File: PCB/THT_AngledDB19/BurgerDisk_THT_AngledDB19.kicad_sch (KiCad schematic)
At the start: 15 parts, among them J1 Daisy port in, J2 MicroSD module, J3 UART, J4 Daisy port out, U1 PC817

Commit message: Wider tracks for power
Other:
- company: (none) -> Colin Leroy-Mira
- title: (none) -> BurgerDisk PCB - Angled DB19 version
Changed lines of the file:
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@@
 (kicad_sch (version 20230121) (generator eeschema)
   (paper "A4")
+  (title_block
+    (title "BurgerDisk PCB - Angled DB19 version")
+    (date "2026-01-28")
+    (rev "v2")
+    (company "Colin Leroy-Mira")
+    (comment 1 "License: CC BY-SA")
+  )
   (junction (at 93.98 90.17) (diameter 0) (color 0 0 0 0)
   )

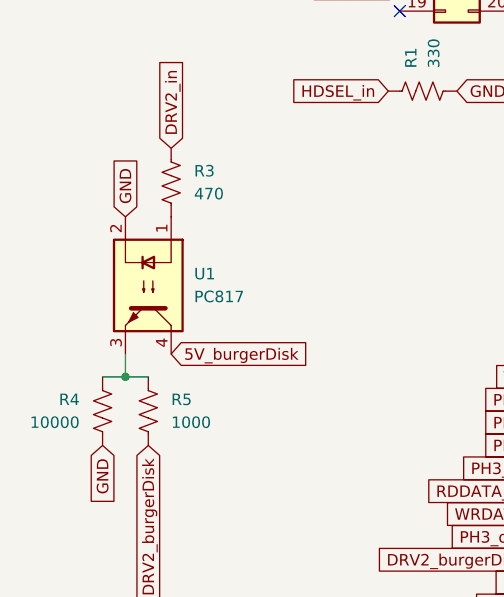
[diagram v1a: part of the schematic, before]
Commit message: Reverse 3 resistors for correct silkscreen orientation
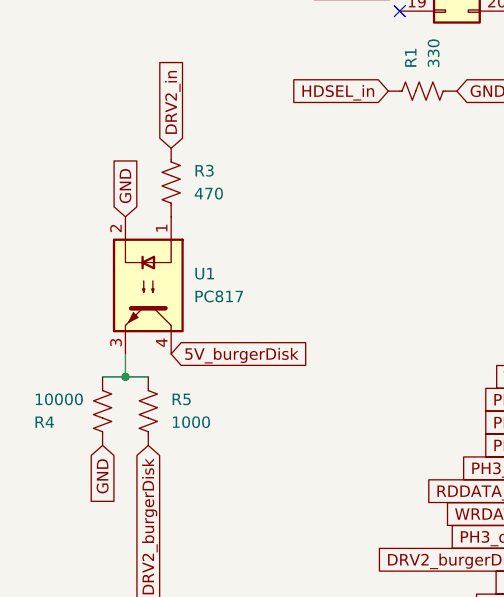
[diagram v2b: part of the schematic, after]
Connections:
- net DRV2_burgerDisk: now also R5.1; no longer R5.2
- net DRV2_in: now also R3.1; no longer R3.2
- net GND: now also R4.1; no longer R4.2
- net at U1.1: now also R3.2; no longer R3.1
- new net: R4.2, R5.2, U1.3
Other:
- moved on the sheet: R3, R4, R5
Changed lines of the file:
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@@
     )
   )
-  (symbol (lib_id "Device:R_US") (at 91.44 93.98 0) (unit 1)
+  (symbol (lib_id "Device:R_US") (at 91.44 93.98 180) (unit 1)
     (in_bom yes) (on_board yes) (dnp no)
-    (property "Reference" "R4" (at 88.9 92.71 0)
-      (effects (font (size 1.27 1.27)) (justify right))
-    )
-    (property "Value" "10000" (at 88.9 95.25 0)
-      (effects (font (size 1.27 1.27)) (justify right))
-    )
-    (property "Footprint" "Resistor_THT:R_Axial_DIN0207_L6.3mm_D2.5mm_P7.62mm_Horizontal" (at 92.456 94.234 90)
+    (property "Reference" "R4" (at 83.82 95.25 0)
+      (effects (font (size 1.27 1.27)) (justify right))
+    )
+    (property "Value" "10000" (at 83.82 92.71 0)
+      (effects (font (size 1.27 1.27)) (justify right))
+    )
+    (property "Footprint" "Resistor_THT:R_Axial_DIN0207_L6.3mm_D2.5mm_P7.62mm_Horizontal" (at 90.424 93.726 90)
       (effects (font (size 1.27 1.27)) hide)
     )
@@
     )
   )
-  (symbol (lib_id "Device:R_US") (at 99.06 68.58 180) (unit 1)
+  (symbol (lib_id "Device:R_US") (at 99.06 68.58 0) (unit 1)
     (in_bom yes) (on_board yes) (dnp no) (fields_autoplaced)
     (property "Reference" "R3" (at 101.6 67.31 0)
-      (effects (font (size 1.27 1.27)) (justify right))
+      (effects (font (size 1.27 1.27)) (justify left))
     )
     (property "Value" "470" (at 101.6 69.85 0)
-      (effects (font (size 1.27 1.27)) (justify right))
-    )
-    (property "Footprint" "Resistor_THT:R_Axial_DIN0309_L9.0mm_D3.2mm_P12.70mm_Horizontal" (at 98.044 68.326 90)
+      (effects (font (size 1.27 1.27)) (justify left))
+    )
+    (property "Footprint" "Resistor_THT:R_Axial_DIN0309_L9.0mm_D3.2mm_P12.70mm_Horizontal" (at 100.076 68.834 90)
       (effects (font (size 1.27 1.27)) hide)
     )
@@
     )
   )
-  (symbol (lib_id "Device:R_US") (at 96.52 93.98 0) (unit 1)
+  (symbol (lib_id "Device:R_US") (at 96.52 93.98 180) (unit 1)
     (in_bom yes) (on_board yes) (dnp no) (fields_autoplaced)
     (property "Reference" "R5" (at 99.06 92.71 0)
-      (effects (font (size 1.27 1.27)) (justify left))
+      (effects (font (size 1.27 1.27)) (justify right))
     )
     (property "Value" "1000" (at 99.06 95.25 0)
-      (effects (font (size 1.27 1.27)) (justify left))
-    )
-    (property "Footprint" "Resistor_THT:R_Axial_DIN0207_L6.3mm_D2.5mm_P7.62mm_Horizontal" (at 97.536 94.234 90)
-      (effects (font (size 1.27 1.27)) hide)
-    )
+      (effects (font (size 1.27 1.27)) (justify right))
+    )
+    (property "Footprint" "Resistor_THT:R_Axial_DIN0207_L6.3mm_D2.5mm_P7.62mm_Horizontal" (at 95.504 93.726 90)
+      (effects (font (size 1.27 1.27)) hide)
+    )

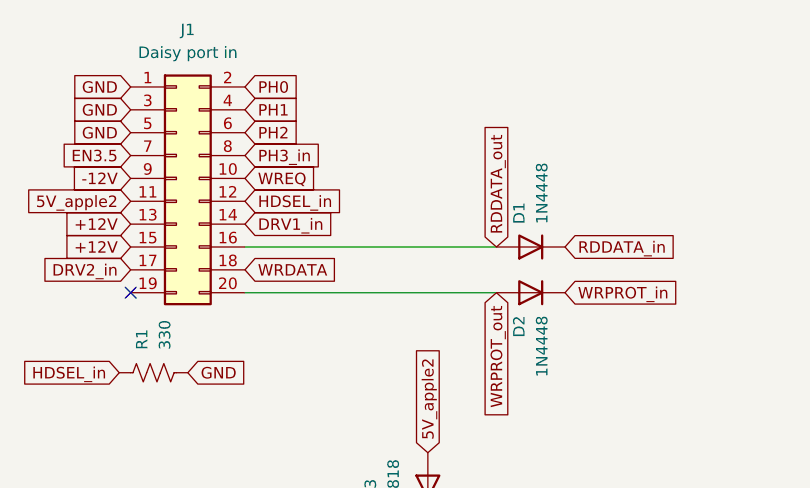
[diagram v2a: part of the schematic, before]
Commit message: Remove RDDATA diode, causing harm on SoftSP
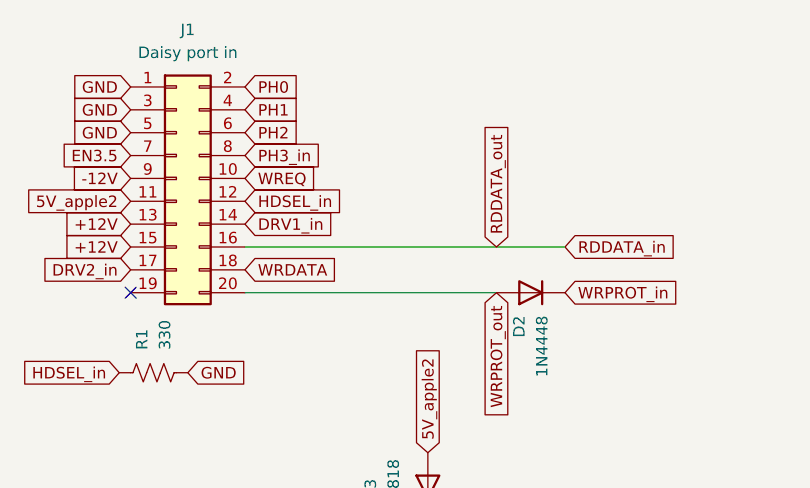
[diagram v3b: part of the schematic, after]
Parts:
- removed D1: 1N4448, Diode_THT:D_DO-35_SOD27_P7.62mm_Horizontal, symbol Diode:1N4448
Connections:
- net RDDATA_out is gone; now on net RDDATA_in: J1.16 (Pin_16), J4.18 (P18)

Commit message: Fix angled DB19 footprint to match the one we can buy
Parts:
- J4: footprint DSUB-19-angled:DSUB-19_Female_Horizontal_P2.77x2.84mm_EdgePinOffset4.94mm_Housed_MountingHolesOffset7.48mm -> DSUB-19-angled:DSUB-19_Female_Horizontal_MXS82009-8251-9246
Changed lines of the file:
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@@
 			)
 		)
-		(property "Footprint" "DSUB-19-angled:DSUB-19_Female_Horizontal_P2.77x2.84mm_EdgePinOffset4.94mm_Housed_MountingHolesOffset7.48mm"
+		(property "Footprint" "DSUB-19-angled:DSUB-19_Female_Horizontal_MXS82009-8251-9246"
 			(at 236.22 116.84 0)
 			(effects

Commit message: Switch to cheaper IDC box header
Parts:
- J1: LCSC C305958 -> C3405
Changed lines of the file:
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@@
 			)
 		)
-		(property "LCSC" "C305958"
+		(property "LCSC" "C3405"
 			(at 129.54 36.83 0)
 			(effects
